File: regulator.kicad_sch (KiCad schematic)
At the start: 6 parts, among them IC1 MAX20029ATIF_V+

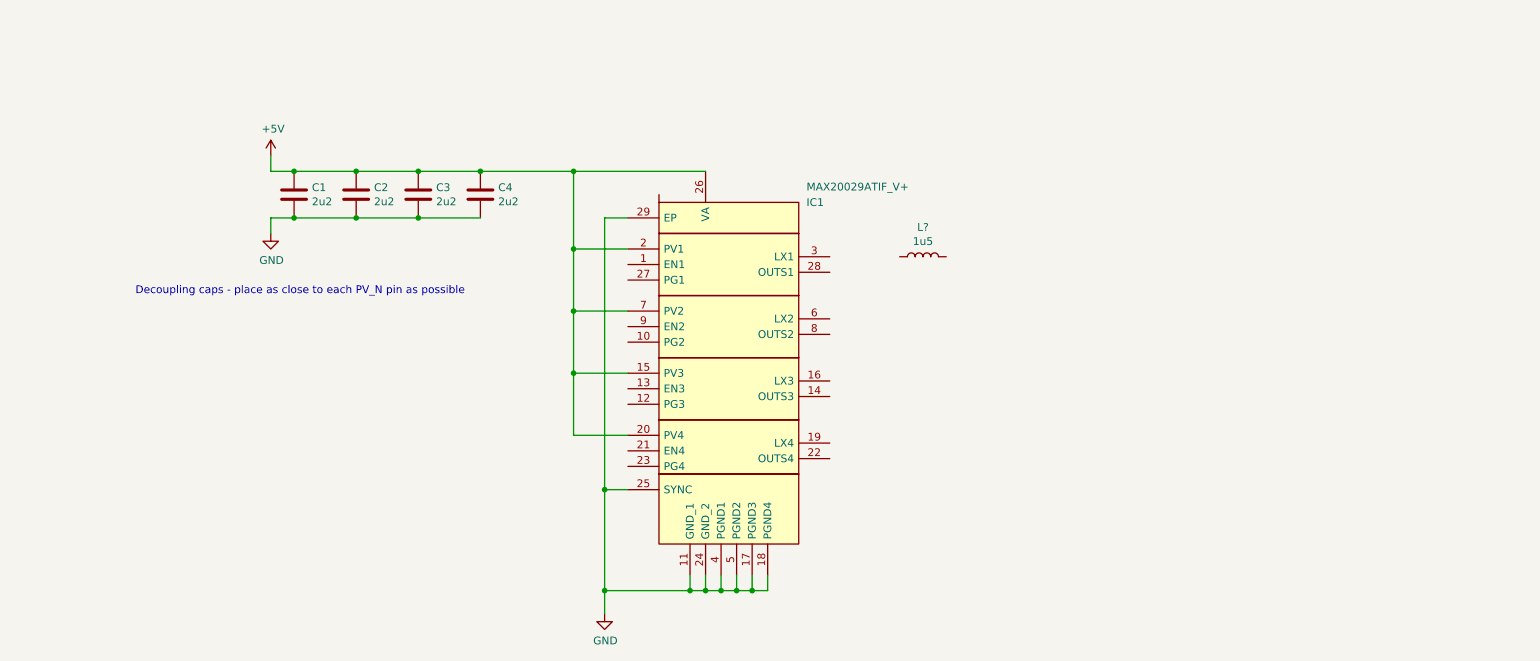
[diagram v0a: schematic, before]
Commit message: Update regulator schematic
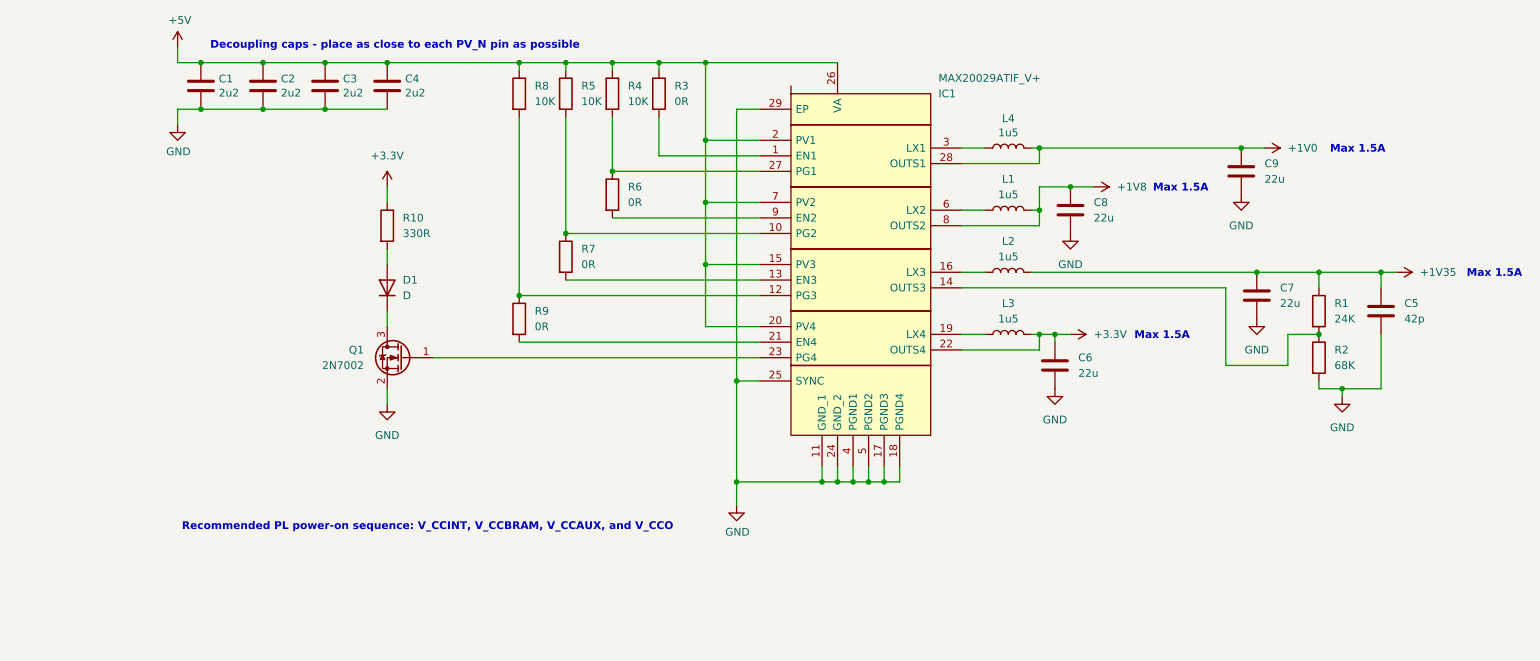
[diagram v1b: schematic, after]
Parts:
- added C5: 42p, symbol Device:C
- added C6, C7, C8, C9: 22u, symbol Device:C
- added D1: D, symbol Device:D
- added L1, L2, L3: 1u5, symbol Device:L
- added Q1: 2N7002, Package_TO_SOT_SMD:SOT-23, symbol Transistor_FET:2N7002
- added R1: 24K, symbol Device:R
- added R10: 330R, symbol Device:R
- added R2: 68K, symbol Device:R
- added R3, R6, R7, R9: 0R, symbol Device:R
- added R4, R5, R8: 10K, symbol Device:R
- gave numbers to parts that had none: 1
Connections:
- net +5V: now also R3.1, R4.1, R5.1, R8.1
- net GND: now also C5.2, C6.2, C7.2, C8.2, C9.2, Q1.2 (S), R2.2
- net at IC1.1 (EN1): now also R3.2
- net at IC1.10 (PG2): now also R5.2, R7.1
- net at IC1.12 (PG3): now also R8.2, R9.1
- net at IC1.13 (EN3): now also R7.2
- net at IC1.14 (OUTS3): now also R1.2, R2.1
- net at IC1.16 (LX3): now also L2.1
- net at IC1.19 (LX4): now also L3.1
- net at IC1.21 (EN4): now also R9.2
- net +3.3V: now reaches IC1.22 (OUTS4)
- net +3.3V: now also C6.1, L3.2, R10.1
- net at IC1.23 (PG4): now also Q1.1 (G)
- net at IC1.27 (PG1): now also R4.2, R6.1
- net +1V0: now reaches IC1.28 (OUTS1)
- net +1V0: now also L4.2, C9.1
- net at IC1.3 (LX1): now also L4.1
- net at IC1.6 (LX2): now also L1.1
- net +1V8: now reaches IC1.8 (OUTS2)
- net +1V8: now also C8.1, L1.2
- net at IC1.9 (EN2): now also R6.2
- new net: D1.1 (K), Q1.3 (D)
- new net: D1.2 (A), R10.2
- new net +1V35: C5.1, C7.1, L2.2, R1.1
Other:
- note added: "Max 1.5A"
- note added: "Recommended PL power-on sequence: V_CCINT, V_CCBRAM, V_CCAUX, and V_CCO"
- moved on the sheet: C1, C2, C3, C4, IC1, L4
